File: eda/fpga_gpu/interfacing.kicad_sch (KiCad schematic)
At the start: 12 parts, among them U3 74HCT541, U4 74HCT541, U5 74HCT541, U6 TXS0108EPW, U7 TXS0108EPW

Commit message: GPU routing
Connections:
- net A0: now also U3.5 (A3); no longer U3.2 (A0)
- net A1: now also U3.4 (A2); no longer U3.3 (A1)
- net A2: now also U3.3 (A1); no longer U3.4 (A2)
- net A3: now also U3.2 (A0); no longer U3.5 (A3)
- net ADev0: now also U7.16 (B4); no longer U7.20 (B1)
- net ADev1: now also U7.17 (B3); no longer U7.18 (B2)
- net ADev2: now also U7.18 (B2); no longer U7.17 (B3)
- net ADev3: now also U7.20 (B1); no longer U7.16 (B4)
- net D0: now also U5.11 (Y7); no longer U5.18 (Y0)
- net D1: now also U5.12 (Y6); no longer U5.17 (Y1)
- net D2: now also U5.13 (Y5); no longer U5.16 (Y2)
- net D3: now also U5.14 (Y4); no longer U5.15 (Y3)
- net D4: now also U5.15 (Y3); no longer U5.14 (Y4)
- net D5: now also U5.16 (Y2); no longer U5.13 (Y5)
- net D6: now also U5.17 (Y1); no longer U5.12 (Y6)
- net D7: now also U5.18 (Y0); no longer U5.11 (Y7)
- net DOut0: now also U5.9 (A7); no longer U5.2 (A0)
- net DOut1: now also U5.8 (A6); no longer U5.3 (A1)
- net DOut2: now also U5.7 (A5); no longer U5.4 (A2)
- net DOut3: now also U5.6 (A4); no longer U5.5 (A3)
- net DOut4: now also U5.5 (A3); no longer U5.6 (A4)
- net DOut5: now also U5.4 (A2); no longer U5.7 (A5)
- net DOut6: now also U5.3 (A1); no longer U5.8 (A6)
- net DOut7: now also U5.2 (A0); no longer U5.9 (A7)
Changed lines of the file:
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@@
     (effects (font (size 1.27 1.27)) (justify left bottom))
   )
-  (label "D3" (at 121.92 54.61 0)
+  (label "D3" (at 121.92 54.61 0) (fields_autoplaced)
     (effects (font (size 1.27 1.27)) (justify left bottom))
   )
-  (label "DIn7" (at 179.07 64.77 0)
+  (label "DIn7" (at 179.07 64.77 0) (fields_autoplaced)
     (effects (font (size 1.27 1.27)) (justify left bottom))
   )
-  (label "D5" (at 102.87 59.69 180) (fields_autoplaced)
+  (label "D2" (at 102.87 59.69 180) (fields_autoplaced)
     (effects (font (size 1.27 1.27)) (justify right bottom))
   )
-  (label "D4" (at 102.87 57.15 180) (fields_autoplaced)
+  (label "D3" (at 102.87 57.15 180) (fields_autoplaced)
     (effects (font (size 1.27 1.27)) (justify right bottom))
   )
-  (label "DIn4" (at 179.07 57.15 0)
+  (label "DIn4" (at 179.07 57.15 0) (fields_autoplaced)
     (effects (font (size 1.27 1.27)) (justify left bottom))
   )
-  (label "A2" (at 123.19 116.84 0)
+  (label "A1" (at 123.19 116.84 0) (fields_autoplaced)
     (effects (font (size 1.27 1.27)) (justify left bottom))
   )
-  (label "DOut4" (at 66.04 57.15 0)
+  (label "DOut3" (at 66.04 57.15 0) (fields_autoplaced)
     (effects (font (size 1.27 1.27)) (justify left bottom))
   )
-  (label "DIn3" (at 179.07 54.61 0)
+  (label "DIn3" (at 179.07 54.61 0) (fields_autoplaced)
     (effects (font (size 1.27 1.27)) (justify left bottom))
   )
-  (label "DIn2" (at 179.07 52.07 0)
+  (label "DIn2" (at 179.07 52.07 0) (fields_autoplaced)
     (effects (font (size 1.27 1.27)) (justify left bottom))
   )
-  (label "ADev1" (at 179.07 114.3 0)
+  (label "ADev2" (at 179.07 114.3 0) (fields_autoplaced)
     (effects (font (size 1.27 1.27)) (justify left bottom))
   )
-  (label "ADev3" (at 179.07 119.38 0)
+  (label "ADev0" (at 179.07 119.38 0) (fields_autoplaced)
     (effects (font (size 1.27 1.27)) (justify left bottom))
   )
-  (label "D1" (at 121.92 49.53 0)
+  (label "D1" (at 121.92 49.53 0) (fields_autoplaced)
     (effects (font (size 1.27 1.27)) (justify left bottom))
   )
-  (label "A0" (at 123.19 111.76 0)
+  (label "A3" (at 123.19 111.76 0) (fields_autoplaced)
     (effects (font (size 1.27 1.27)) (justify left bottom))
   )
-  (label "DOut6" (at 66.04 62.23 0)
+  (label "DOut1" (at 66.04 62.23 0) (fields_autoplaced)
     (effects (font (size 1.27 1.27)) (justify left bottom))
   )
-  (label "DIn6" (at 179.07 62.23 0)
+  (label "DIn6" (at 179.07 62.23 0) (fields_autoplaced)
     (effects (font (size 1.27 1.27)) (justify left bottom))
   )
-  (label "DOut1" (at 66.04 49.53 0)
+  (label "DOut6" (at 66.04 49.53 0) (fields_autoplaced)
     (effects (font (size 1.27 1.27)) (justify left bottom))
   )
-  (label "DOut2" (at 66.04 52.07 0)
+  (label "DOut5" (at 66.04 52.07 0) (fields_autoplaced)
     (effects (font (size 1.27 1.27)) (justify left bottom))
   )
-  (label "D0" (at 121.92 46.99 0)
+  (label "D0" (at 121.92 46.99 0) (fields_autoplaced)
     (effects (font (size 1.27 1.27)) (justify left bottom))
   )
-  (label "D4" (at 121.92 57.15 0)
+  (label "D4" (at 121.92 57.15 0) (fields_autoplaced)
     (effects (font (size 1.27 1.27)) (justify left bottom))
   )
-  (label "ADev0" (at 179.07 111.76 0)
+  (label "ADev3" (at 179.07 111.76 0) (fields_autoplaced)
     (effects (font (size 1.27 1.27)) (justify left bottom))
   )
-  (label "D1" (at 102.87 49.53 180) (fields_autoplaced)
+  (label "D6" (at 102.87 49.53 180) (fields_autoplaced)
     (effects (font (size 1.27 1.27)) (justify right bottom))
   )
-  (label "A3" (at 123.19 119.38 0)
+  (label "A0" (at 123.19 119.38 0) (fields_autoplaced)
     (effects (font (size 1.27 1.27)) (justify left bottom))
   )
-  (label "DOut5" (at 66.04 59.69 0)
+  (label "DOut2" (at 66.04 59.69 0) (fields_autoplaced)
     (effects (font (size 1.27 1.27)) (justify left bottom))
   )
-  (label "DIn5" (at 179.07 59.69 0)
+  (label "DIn5" (at 179.07 59.69 0) (fields_autoplaced)
     (effects (font (size 1.27 1.27)) (justify left bottom))
   )
-  (label "D2" (at 102.87 52.07 180) (fields_autoplaced)
+  (label "D5" (at 102.87 52.07 180) (fields_autoplaced)
     (effects (font (size 1.27 1.27)) (justify right bottom))
   )
-  (label "D7" (at 102.87 64.77 180) (fields_autoplaced)
+  (label "D0" (at 102.87 64.77 180) (fields_autoplaced)
     (effects (font (size 1.27 1.27)) (justify right bottom))
   )
-  (label "A1" (at 123.19 114.3 0)
+  (label "A2" (at 123.19 114.3 0) (fields_autoplaced)
     (effects (font (size 1.27 1.27)) (justify left bottom))
   )
-  (label "D2" (at 121.92 52.07 0)
+  (label "D2" (at 121.92 52.07 0) (fields_autoplaced)
     (effects (font (size 1.27 1.27)) (justify left bottom))
   )
-  (label "DOut7" (at 66.04 64.77 0)
+  (label "DOut0" (at 66.04 64.77 0) (fields_autoplaced)
     (effects (font (size 1.27 1.27)) (justify left bottom))
   )
-  (label "DOut3" (at 66.04 54.61 0)
+  (label "DOut4" (at 66.04 54.61 0) (fields_autoplaced)
     (effects (font (size 1.27 1.27)) (justify left bottom))
   )
-  (label "DIn0" (at 179.07 46.99 0)
+  (label "DIn0" (at 179.07 46.99 0) (fields_autoplaced)
     (effects (font (size 1.27 1.27)) (justify left bottom))
   )
-  (label "DIn1" (at 179.07 49.53 0)
+  (label "DIn1" (at 179.07 49.53 0) (fields_autoplaced)
     (effects (font (size 1.27 1.27)) (justify left bottom))
   )
-  (label "D0" (at 102.87 46.99 180) (fields_autoplaced)
+  (label "D7" (at 102.87 46.99 180) (fields_autoplaced)
     (effects (font (size 1.27 1.27)) (justify right bottom))
   )
-  (label "D6" (at 121.92 62.23 0)
+  (label "D6" (at 121.92 62.23 0) (fields_autoplaced)
     (effects (font (size 1.27 1.27)) (justify left bottom))
   )
-  (label "DOut0" (at 66.04 46.99 0)
+  (label "DOut7" (at 66.04 46.99 0) (fields_autoplaced)
     (effects (font (size 1.27 1.27)) (justify left bottom))
   )
-  (label "ADev2" (at 179.07 116.84 0)
+  (label "ADev1" (at 179.07 116.84 0) (fields_autoplaced)
     (effects (font (size 1.27 1.27)) (justify left bottom))
   )
-  (label "D5" (at 121.92 59.69 0)
+  (label "D5" (at 121.92 59.69 0) (fields_autoplaced)
     (effects (font (size 1.27 1.27)) (justify left bottom))
   )
-  (label "D6" (at 102.87 62.23 180) (fields_autoplaced)
+  (label "D1" (at 102.87 62.23 180) (fields_autoplaced)
     (effects (font (size 1.27 1.27)) (justify right bottom))
   )
-  (label "D7" (at 121.92 64.77 0)
+  (label "D7" (at 121.92 64.77 0) (fields_autoplaced)
     (effects (font (size 1.27 1.27)) (justify left bottom))
   )
-  (label "D3" (at 102.87 54.61 180) (fields_autoplaced)
+  (label "D4" (at 102.87 54.61 180) (fields_autoplaced)
     (effects (font (size 1.27 1.27)) (justify right bottom))
   )

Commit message: More routing on the GPU board
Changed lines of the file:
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@@
+    (stroke (width 0) (type default))
+  )
+  (wire (pts (xy 110.49 134.62) (xy 116.84 134.62))
     (stroke (width 0) (type default))
   )
@@
     (effects (font (size 1.27 1.27)) (justify left))
   )
+  (hierarchical_label "~{IRQ}" (shape output) (at 116.84 134.62 0) (fields_autoplaced)
+    (effects (font (size 1.27 1.27)) (justify left))
+  )

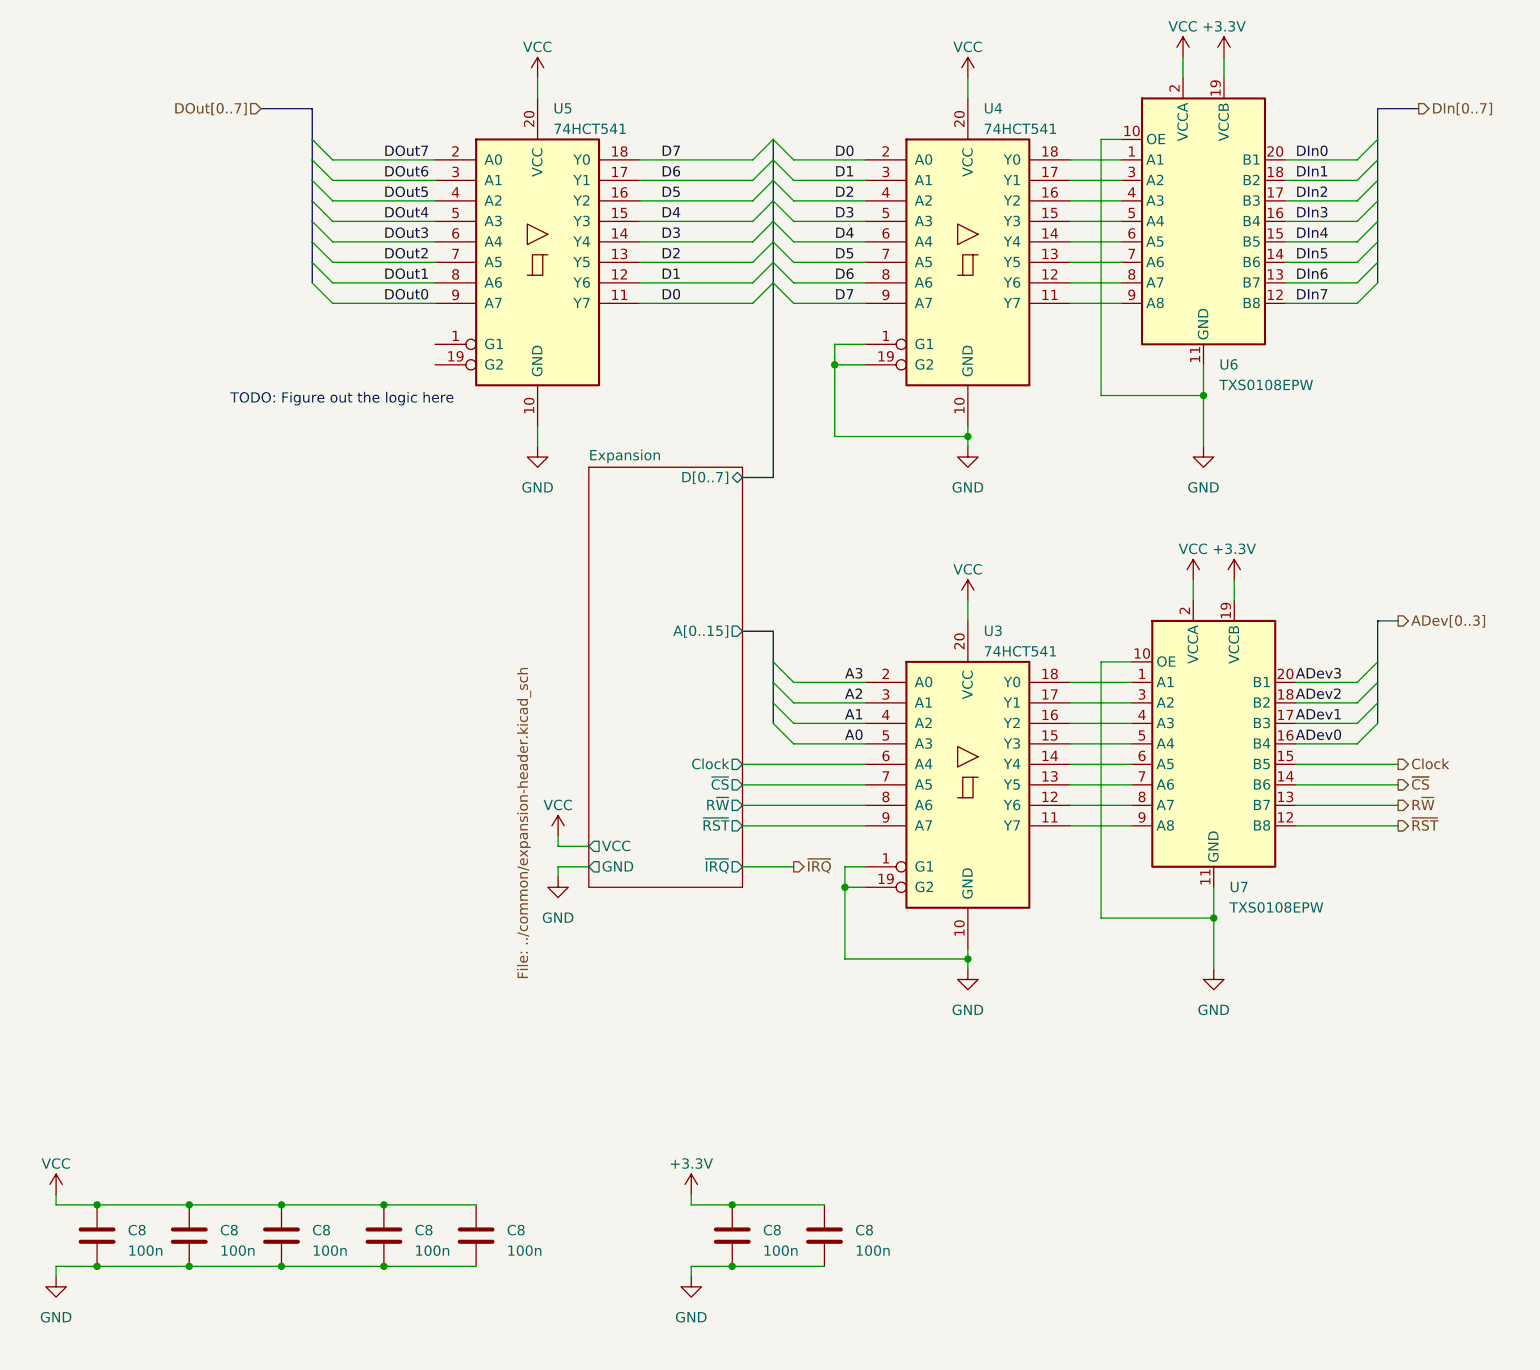
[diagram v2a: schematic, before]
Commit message: Add expansion backplane
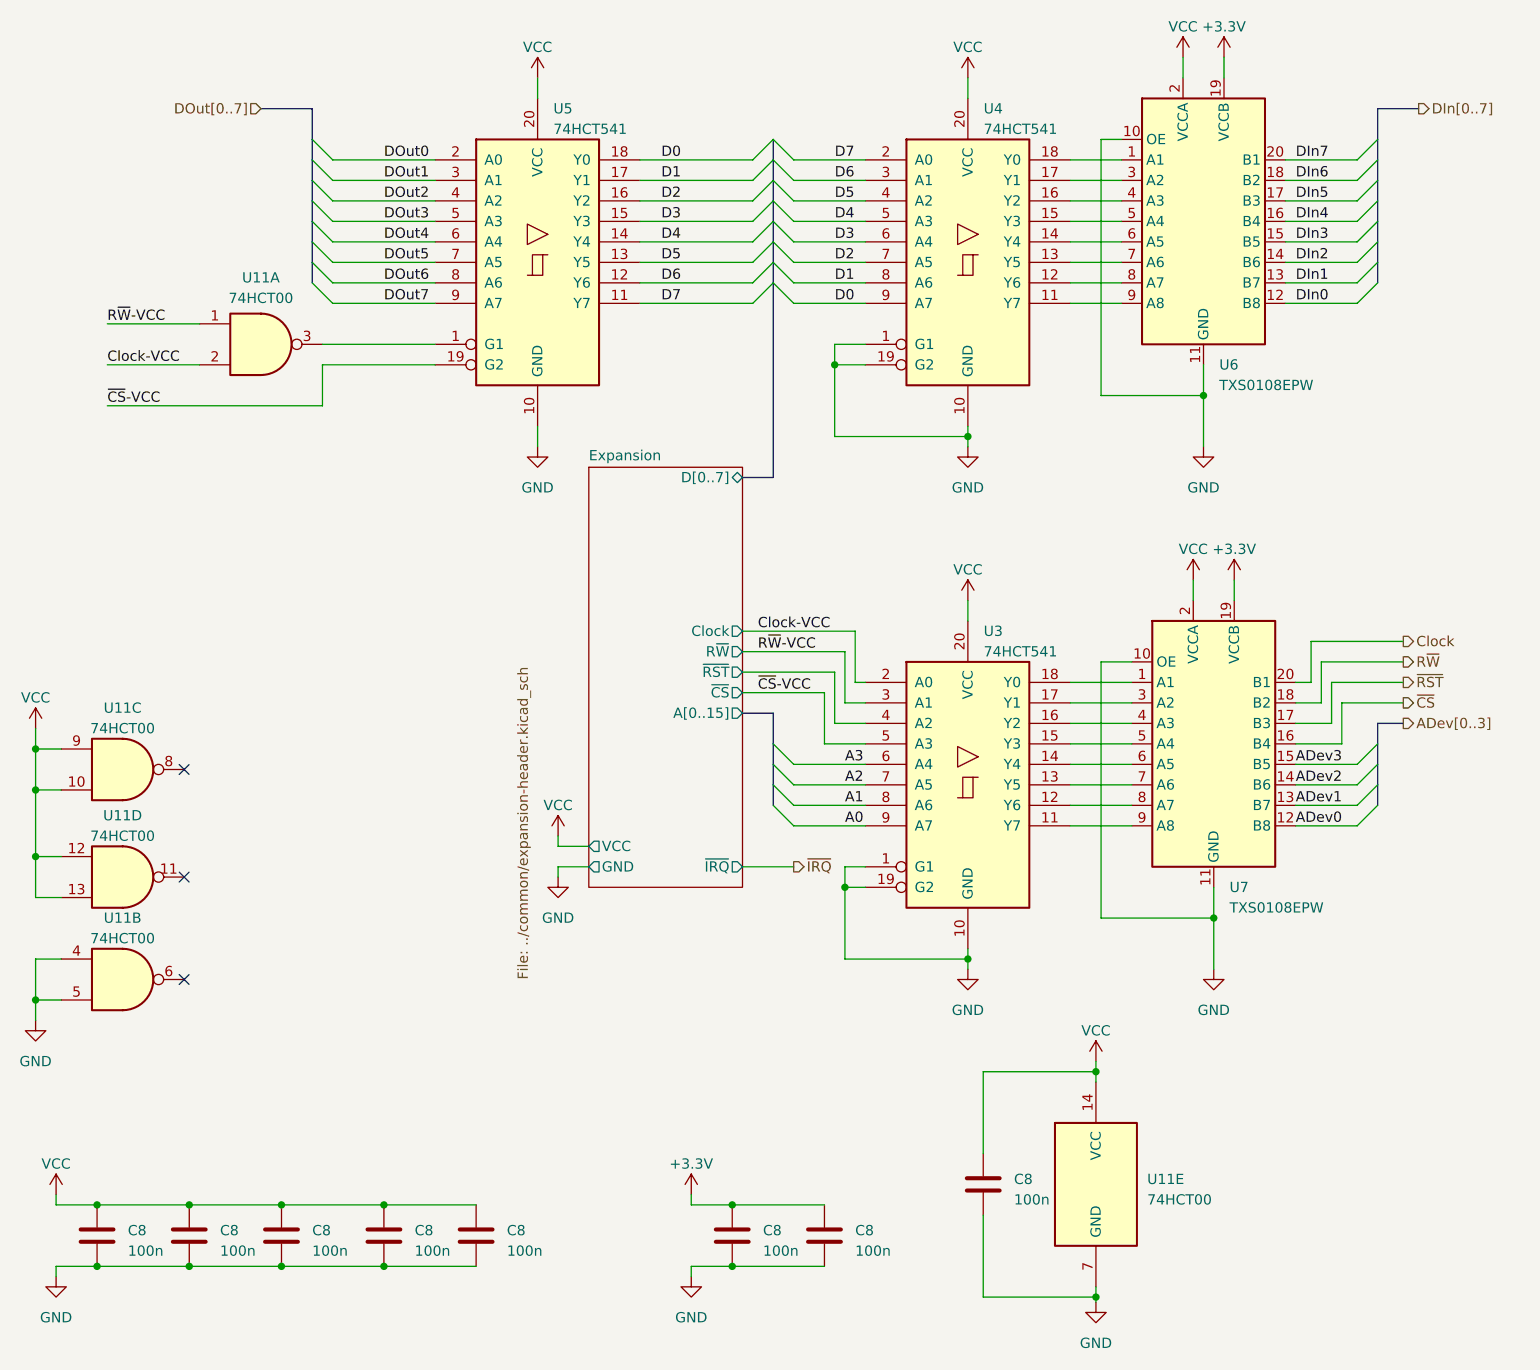
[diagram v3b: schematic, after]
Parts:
- added C8: 100n, Capacitor_SMD:C_0805_2012Metric, symbol Device:C
- added U11: 74HCT00, Package_SO:SSOP-14_5.3x6.2mm_P0.65mm, symbol 74xx:74HCT00
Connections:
- net Expansion/Clock is gone; now on net A3: U3.6 (A4)
- net Expansion/R~{W} is gone; now on net A1: U3.8 (A6)
- net Expansion/~{CS} is gone; now on net A2: U3.7 (A5)
- net A0: now also U3.9 (A7); no longer U3.5 (A3)
- net A1: no longer U3.4 (A2)
- net A2: no longer U3.3 (A1)
- net A3: no longer U3.2 (A0)
- net ADev0: now also U7.12 (B8); no longer U7.16 (B4)
- net ADev1: now also U7.13 (B7); no longer U7.17 (B3)
- net ADev2: now also U7.14 (B6); no longer U7.18 (B2)
- net ADev3: now also U7.15 (B5); no longer U7.20 (B1)
- net Clock: now also U7.20 (B1); no longer U7.15 (B5)
- net D0: now also U4.9 (A7), U5.18 (Y0); no longer U4.2 (A0), U5.11 (Y7)
- net D1: now also U4.8 (A6), U5.17 (Y1); no longer U4.3 (A1), U5.12 (Y6)
- net D2: now also U4.7 (A5), U5.16 (Y2); no longer U4.4 (A2), U5.13 (Y5)
- net D3: now also U4.6 (A4), U5.15 (Y3); no longer U4.5 (A3), U5.14 (Y4)
- net D4: now also U4.5 (A3), U5.14 (Y4); no longer U4.6 (A4), U5.15 (Y3)
- net D5: now also U4.4 (A2), U5.13 (Y5); no longer U4.7 (A5), U5.16 (Y2)
- net D6: now also U4.3 (A1), U5.12 (Y6); no longer U4.8 (A6), U5.17 (Y1)
- net D7: now also U4.2 (A0), U5.11 (Y7); no longer U4.9 (A7), U5.18 (Y0)
- net DIn0: now also U6.12 (B8); no longer U6.20 (B1)
- net DIn1: now also U6.13 (B7); no longer U6.18 (B2)
- net DIn2: now also U6.14 (B6); no longer U6.17 (B3)
- net DIn3: now also U6.15 (B5); no longer U6.16 (B4)
- net DIn4: now also U6.16 (B4); no longer U6.15 (B5)
- net DIn5: now also U6.17 (B3); no longer U6.14 (B6)
- net DIn6: now also U6.18 (B2); no longer U6.13 (B7)
- net DIn7: now also U6.20 (B1); no longer U6.12 (B8)
- net DOut0: now also U5.2 (A0); no longer U5.9 (A7)
- net DOut1: now also U5.3 (A1); no longer U5.8 (A6)
- net DOut2: now also U5.4 (A2); no longer U5.7 (A5)
- net DOut3: now also U5.5 (A3); no longer U5.6 (A4)
- net DOut4: now also U5.6 (A4); no longer U5.5 (A3)
- net DOut5: now also U5.7 (A5); no longer U5.4 (A2)
- net DOut6: now also U5.8 (A6); no longer U5.3 (A1)
- net DOut7: now also U5.9 (A7); no longer U5.2 (A0)
- net Expansion/~{RST}: now also U3.4 (A2); no longer U3.9 (A7)
- net GND: now also C8.2, U11.4, U11.5, U11.7 (GND)
- net R~{W}: now also U7.18 (B2); no longer U7.13 (B7)
- net VCC: now also C8.1, U11.10, U11.12, U11.13, U11.14 (VCC), U11.9
- net ~{CS}: now also U7.16 (B4); no longer U7.14 (B6)
- net ~{RST}: now also U7.17 (B3); no longer U7.12 (B8)
- net at U5.1 (G1): now also U11.3
- net ~{CS}-VCC: now reaches U5.19 (G2)
- net ~{CS}-VCC: now also U3.5 (A3)
- new net Clock-VCC: U11.2, U3.2 (A0)
- new net R~{W}-VCC: U11.1, U3.3 (A1)
- no-connect marks 0 -> 3
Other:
- note removed: "TODO: Figure out the logic here"
